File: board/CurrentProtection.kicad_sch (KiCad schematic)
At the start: 26 parts, among them Q4 IPB180N10S4-02, Q9 IPB180N10S4-02, U10 ACS72981LLRATR-100U3, U2 LM5050MK-1_NOPB, U3 LM5050MK-1_NOPB

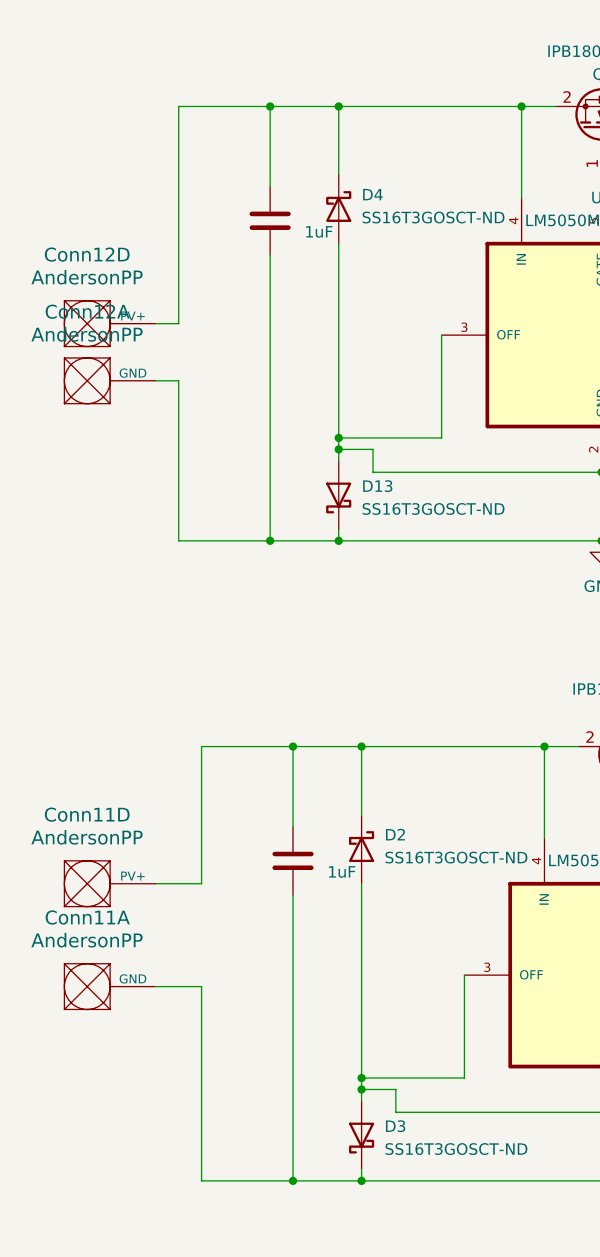
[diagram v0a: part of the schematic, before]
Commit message: new connectors
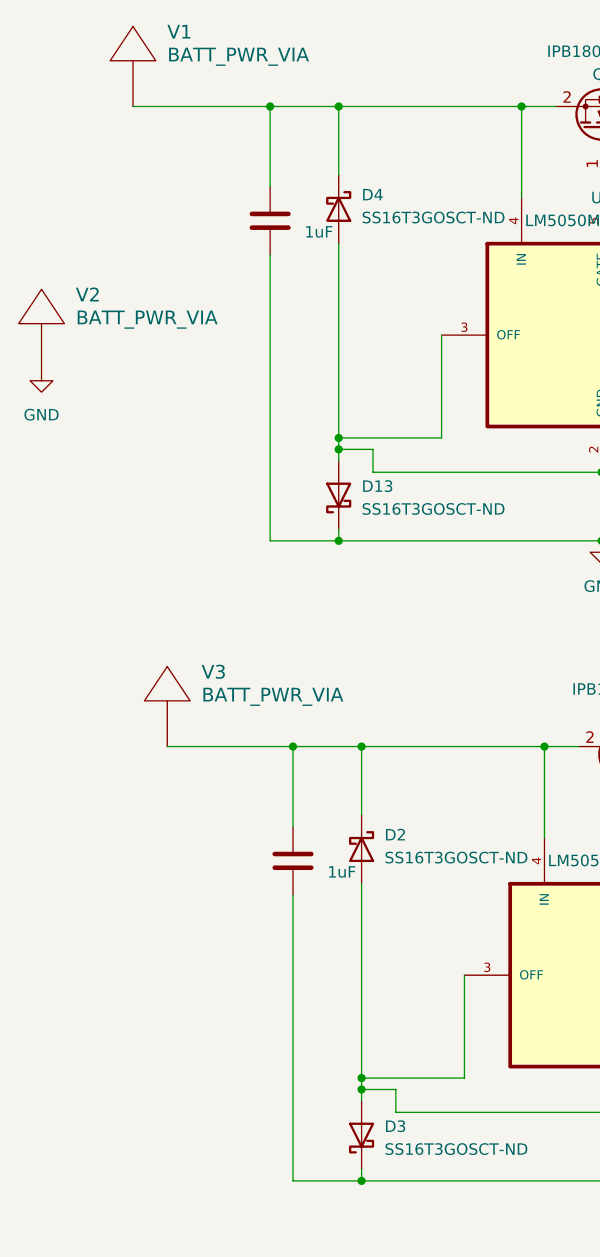
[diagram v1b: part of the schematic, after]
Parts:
- removed Conn11, Conn12: AndersonPP, MRDT_Connectors:Square_Anderson_2_H_Side_By_Side_PV, symbol MRDT_Connectors:AndersonPP
- added V1, V2, V3: BATT_PWR_VIA, MRDT_Drill_Holes:BATT_PWR_VIA, symbol MRDT_Drill_Holes:BATT_PWR_VIA
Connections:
- net GND: now also V2.1
- net at C11.1, D4.1 (K), Q4.2 (S)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: now also V1.1
- net at C5.1, D2.1 (K), Q9.2 (S)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: now also V3.1

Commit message: Deleted Capacitors
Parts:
- removed C13, C4: 22uF, Capacitor_SMD:C_0603_1608Metric_Pad1.08x0.95mm_HandSolder, symbol Device:C
- added C13, C24, C4: 1000uF, Capacitor_THT:CP_Radial_D16.0mm_P7.50mm, symbol Device:C_Polarized_US
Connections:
- net GND: now also C13.2, C24.2, C4.2
- net at D14.1 (K), D5.1 (K), Q4.4 (D)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: now also C13.1, C24.1, C4.1
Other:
- moved on the sheet: C1, C2, R1, U10

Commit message: experimented with layout
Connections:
- net Batt2: now reaches C5.1, D2.1 (K), Q9.2 (S), Q9.3 (S), Q9.5 (S), Q9.6 (S), Q9.7 (S), U3.4 (IN), V3.1
- net Batt1: now reaches C11.1, D4.1 (K), Q4.2 (S), Q4.3 (S), Q4.5 (S), Q4.6 (S), Q4.7 (S), U2.4 (IN), V1.1
- net Batt_to_CS: now reaches C13.1, C24.1, C4.1, D14.1 (K), D5.1 (K), Q4.4 (D), Q9.4 (D), R2.2, R39.2, U10.5 (IP+), U2.6 (OUT), U3.6 (OUT)
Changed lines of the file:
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@@
+		)
+	)
+	(label "Batt_to_CS"
+		(at 199.39 73.66 0)
+		(effects
+			(font
+				(size 1.27 1.27)
+			)
+			(justify left bottom)
+		)
+	)
+	(label "Batt1"
+		(at 33.02 73.66 0)
+		(effects
+			(font
+				(size 1.27 1.27)
+			)
+			(justify left bottom)
+		)
+	)
+	(label "Batt2"
+		(at 35.56 144.78 0)
+		(effects
+			(font
+				(size 1.27 1.27)
+			)
+			(justify left bottom)
 		)
 	)

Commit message: do basically everything
12 hours of our life
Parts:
- removed C10, C12: 0.1uF, Capacitor_SMD:C_0603_1608Metric_Pad1.08x0.95mm_HandSolder, symbol Device:C
- removed C11, C5: 1uF, Capacitor_SMD:C_0603_1608Metric_Pad1.08x0.95mm_HandSolder, symbol Device:C
- removed D13, D2, D3, D4: SS16T3GOSCT-ND, Diode_SMD:D_SMA, symbol Diode:SS16
- removed D14, D5: SMBJ60AFSTR-ND, Diode_SMD:D_SMB, symbol Diode:SS16
- removed Q4, Q9: IPB180N10S4-02, Package_TO_SOT_SMD:TO-263-6, symbol Transistor_FET:IPB180N10S4-02
- removed R2: R_US, Resistor_SMD:R_0603_1608Metric_Pad0.98x0.95mm_HandSolder, symbol Device:R_US
- removed R39: 100, Resistor_SMD:R_0603_1608Metric_Pad0.98x0.95mm_HandSolder, symbol Device:R_US
- removed U2, U3: LM5050MK-1_NOPB, PowerManagementBoard:SOT95P280X110-6N, symbol LM5050MK-1_NOPB:LM5050MK-1_NOPB
- removed V3: BATT_PWR_VIA, MRDT_Drill_Holes:BATT_PWR_VIA, symbol MRDT_Drill_Holes:BATT_PWR_VIA
- added TP1: TestPoint, Connector_Pin:Pin_D1.1mm_L10.2mm_W3.5mm_Flat, symbol Connector:TestPoint
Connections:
- net Batt_to_CS is gone; now on net Batt1: C13.1, C24.1, C4.1, U10.5 (IP+)
- net +24V: now also TP1.1

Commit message: 17 hours of our lives
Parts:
- D6: value GRNLED -> GRN
- TP1: footprint Connector_Pin:Pin_D1.1mm_L10.2mm_W3.5mm_Flat -> TestPoint:TestPoint_Pad_D1.0mm
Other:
- moved on the sheet: V1
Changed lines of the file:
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@@
+	)
+	(junction
+		(at 260.35 88.9)
+		(diameter 0)
+		(color 0 0 0 0)
+	)
+	(junction
+		(at 168.91 81.28)
+		(diameter 0)
+		(color 0 0 0 0)
+	)
+	(junction
+		(at 168.91 73.66)
+		(diameter 0)
+		(color 0 0 0 0)
 	)
 	(junction
@@
 	)
 	(junction
-		(at 260.35 88.9)
-		(diameter 0)
-		(color 0 0 0 0)
-	)
-	(junction
-		(at 168.91 81.28)
-		(diameter 0)
-		(color 0 0 0 0)
-	)
-	(junction
-		(at 168.91 73.66)
-		(diameter 0)
-		(color 0 0 0 0)
-	)
-	(junction
 		(at 241.3 109.22)
 		(diameter 0)
@@
 	(wire
 		(pts
+			(xy 153.67 73.66) (xy 63.5 73.66)
+		)
+		(stroke
+			(width 0)
+			(type default)
+		)
+	)
+	(wire
+		(pts
 			(xy 168.91 73.66) (xy 182.88 73.66)
 		)
@@
 		(pts
 			(xy 264.16 109.22) (xy 264.16 110.49)
-		)
-		(stroke
-			(width 0)
-			(type default)
-		)
-	)
-	(wire
-		(pts
-			(xy 26.67 73.66) (xy 153.67 73.66)
 		)
 		(stroke
@@
 	)
 	(label "Batt1"
-		(at 33.02 73.66 0)
+		(at 153.67 73.66 0)
 		(effects
 			(font
@@
 			)
 		)
-		(property "Value" "GRNLED"
+		(property "Value" "GRN"
 			(at 190.8175 137.16 0)
 			(effects
@@
 			)
 		)
-		(property "Footprint" "Connector_Pin:Pin_D1.1mm_L10.2mm_W3.5mm_Flat"
+		(property "Footprint" "TestPoint:TestPoint_Pad_D1.0mm"
 			(at 214.63 101.6 0)
 			(effects
@@
 	(symbol
 		(lib_id "MRDT_Drill_Holes:BATT_PWR_VIA")
-		(at 26.67 68.58 0)
+		(at 63.5 68.58 0)
 		(unit 1)
 		(exclude_from_sim no)
@@
 		(fields_autoplaced yes)
 		(property "Reference" "V1"
-			(at 30.48 65.4049 0)
+			(at 67.31 65.4049 0)
 			(effects
 				(font
@@
 		)
 		(property "Value" "BATT_PWR_VIA"
-			(at 30.48 67.9449 0)
+			(at 67.31 67.9449 0)
 			(effects
 				(font
@@
 		)
 		(property "Footprint" "MRDT_Drill_Holes:BATT_PWR_VIA"
-			(at 26.67 68.58 0)
+			(at 63.5 68.58 0)
 			(effects
 				(font
@@
 		)
 		(property "Datasheet" ""
-			(at 26.67 68.58 0)
+			(at 63.5 68.58 0)
 			(effects
 				(font
@@
 		)
 		(property "Description" ""
-			(at 26.67 68.58 0)
-			(effects
-				(font
+			(at 63.5 68.58 0)
+			(effects
+				(font

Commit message: 18 Hours and counting...
-Moved LEDs,
-Added innocent kitties
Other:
- moved on the sheet: V1
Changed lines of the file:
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@@
 	(wire
 		(pts
-			(xy 153.67 73.66) (xy 63.5 73.66)
+			(xy 153.67 73.66) (xy 140.97 73.66)
 		)
 		(stroke
@@
 	(symbol
 		(lib_id "MRDT_Drill_Holes:BATT_PWR_VIA")
-		(at 63.5 68.58 0)
+		(at 140.97 68.58 0)
 		(unit 1)
 		(exclude_from_sim no)
@@
 		(fields_autoplaced yes)
 		(property "Reference" "V1"
-			(at 67.31 65.4049 0)
+			(at 144.78 65.4049 0)
 			(effects
 				(font
@@
 		)
 		(property "Value" "BATT_PWR_VIA"
-			(at 67.31 67.9449 0)
+			(at 144.78 67.9449 0)
 			(effects
 				(font
@@
 		)
 		(property "Footprint" "MRDT_Drill_Holes:BATT_PWR_VIA"
-			(at 63.5 68.58 0)
+			(at 140.97 68.58 0)
 			(effects
 				(font
@@
 		)
 		(property "Datasheet" ""
-			(at 63.5 68.58 0)
+			(at 140.97 68.58 0)
 			(effects
 				(font
@@
 		)
 		(property "Description" ""
-			(at 63.5 68.58 0)
-			(effects
-				(font
+			(at 140.97 68.58 0)
+			(effects
+				(font

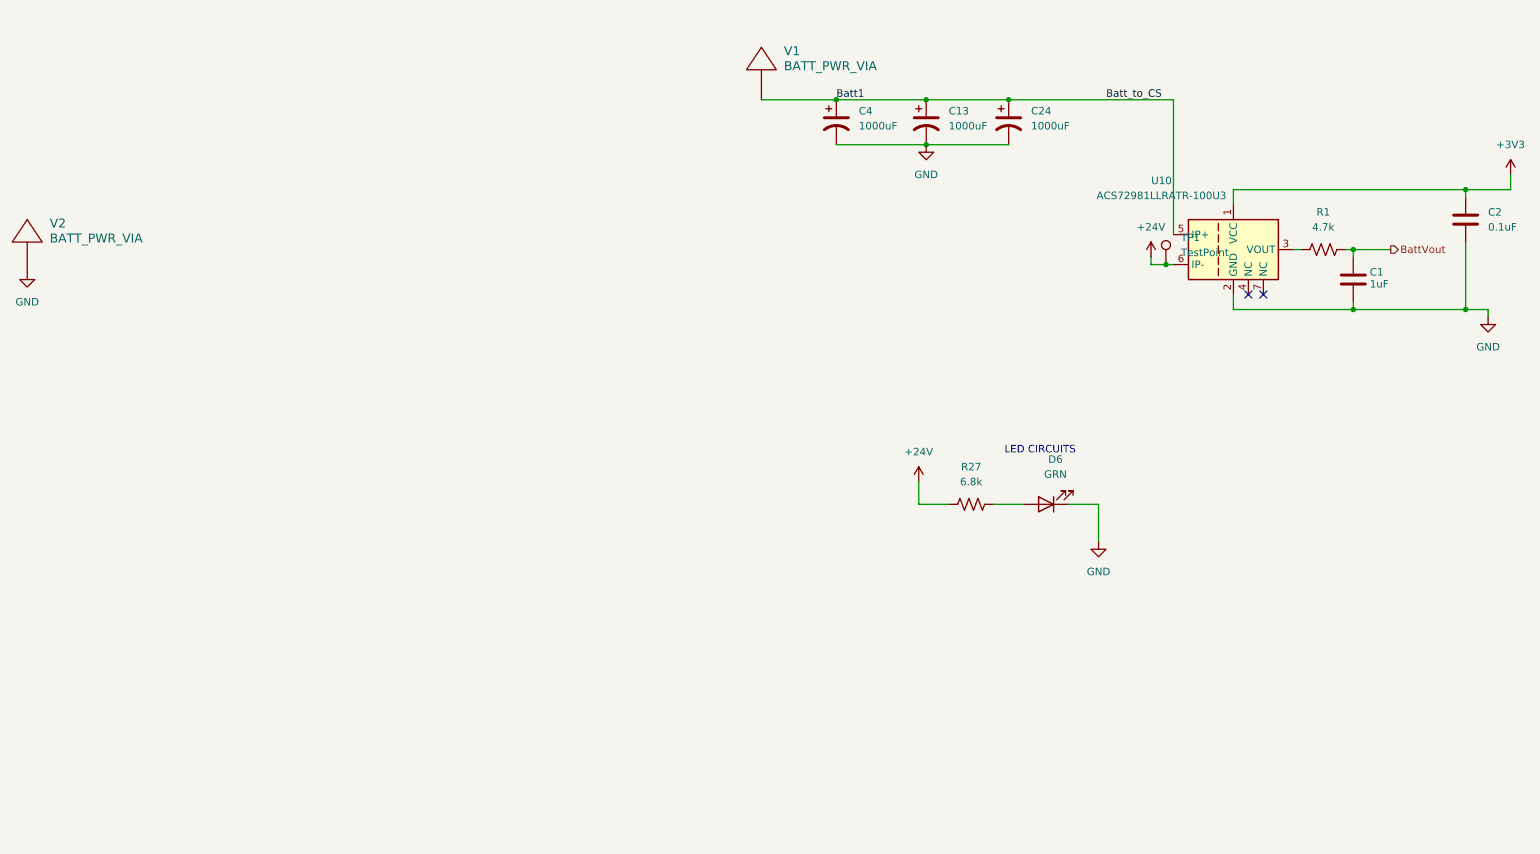
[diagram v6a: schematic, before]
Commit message: Center schematics and layout for prettiness
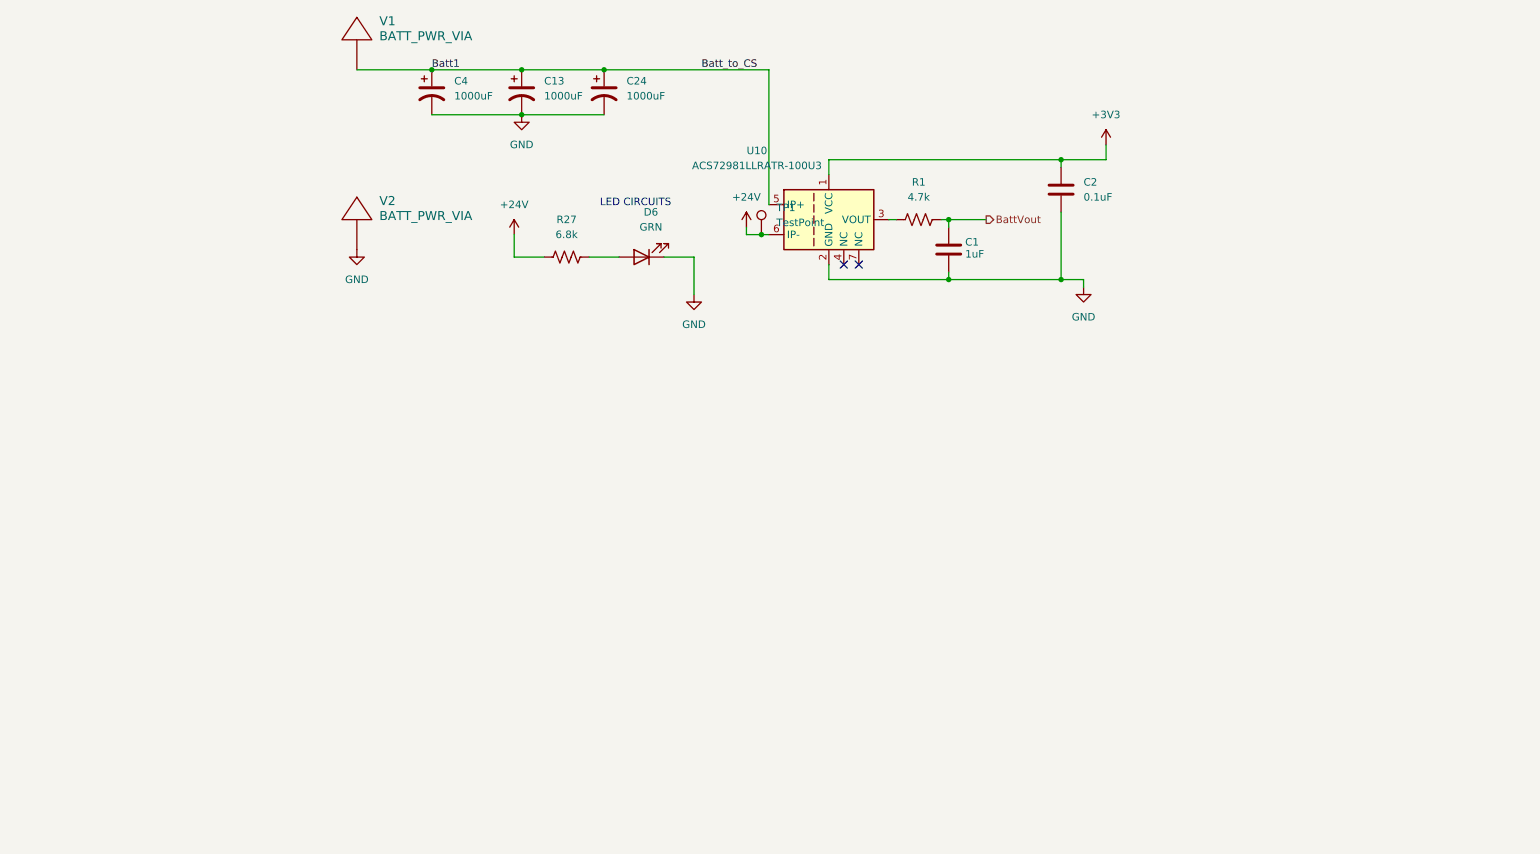
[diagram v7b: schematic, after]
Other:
- moved on the sheet: C1, C13, C2, C24, C4, D6, R1, R27, TP1, U10, V1, V2

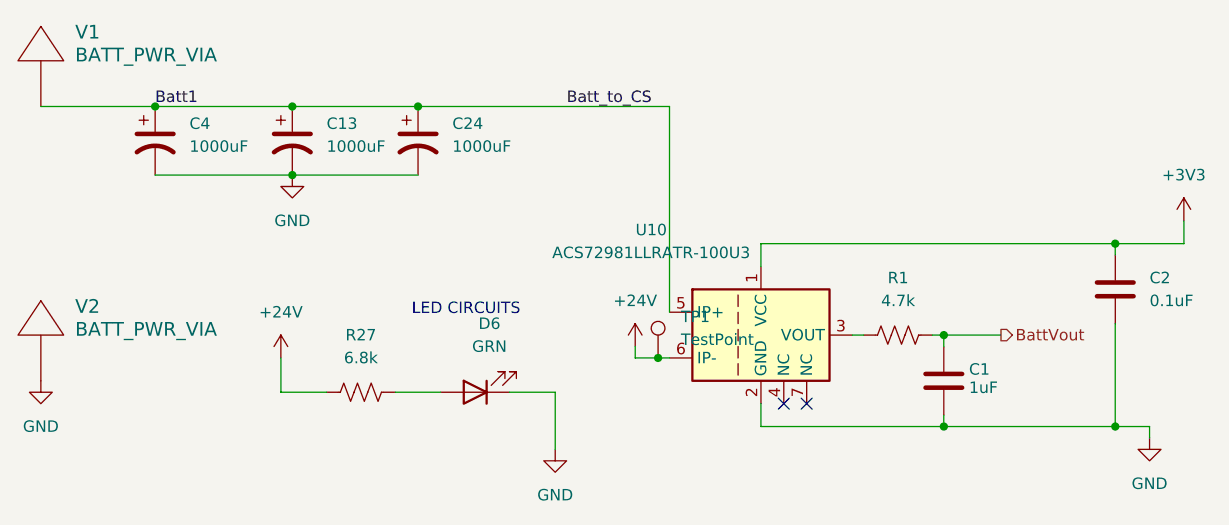
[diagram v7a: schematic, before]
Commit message: add label for battery sensing molex connector
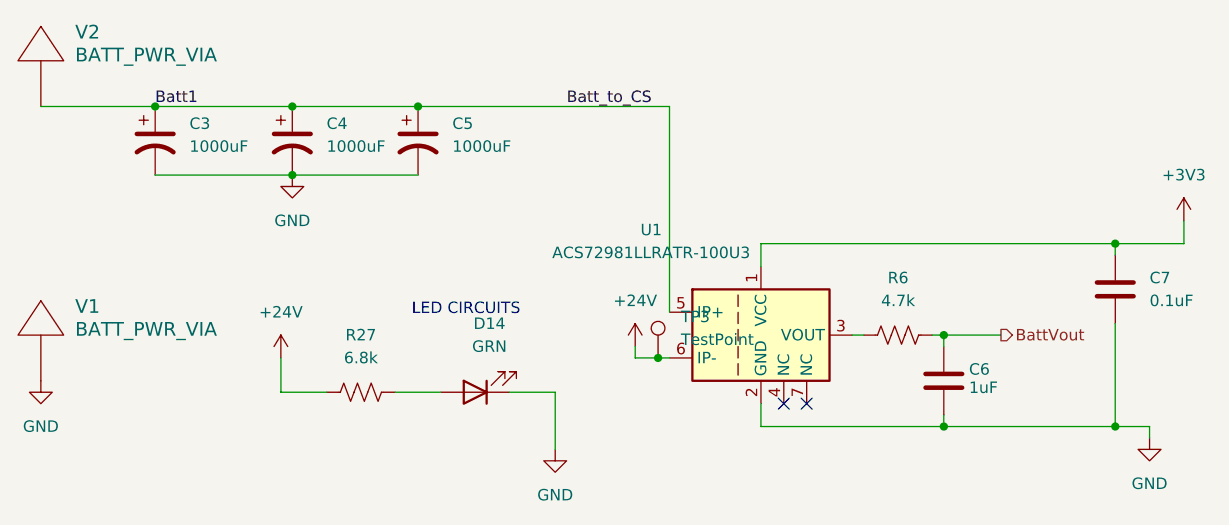
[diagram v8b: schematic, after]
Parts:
- renumbered C4 to C3, C13 to C4, C24 to C5, C1 to C6, C2 to C7, D6 to D14, R1 to R6, TP1 to TP3, U10 to U1, V2 to V1, V1 to V2
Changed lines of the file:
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@@
 		(dnp no)
 		(fields_autoplaced yes)
-		(property "Reference" "C2"
+		(property "Reference" "C7"
 			(at 195.58 87.6299 0)
 			(effects
@@
 			(project ""
 				(path "/7eaa639d-7062-45e7-be05-1c2855431307/fa17e088-8bc3-4875-b327-c5ed0adaa270"
-					(reference "C2")
+					(reference "C7")
 					(unit 1)
 				)
@@
 		(dnp no)
 		(fields_autoplaced yes)
-		(property "Reference" "C24"
+		(property "Reference" "C5"
 			(at 118.11 70.4849 0)
 			(effects
@@
 			(project "PowerManagementBoard"
 				(path "/7eaa639d-7062-45e7-be05-1c2855431307/fa17e088-8bc3-4875-b327-c5ed0adaa270"
-					(reference "C24")
+					(reference "C5")
 					(unit 1)
 				)
@@
 		(dnp no)
 		(fields_autoplaced yes)
-		(property "Reference" "D6"
+		(property "Reference" "D14"
 			(at 122.2375 92.71 0)
 			(effects
@@
 			(project "PowerManagementBoard"
 				(path "/7eaa639d-7062-45e7-be05-1c2855431307/fa17e088-8bc3-4875-b327-c5ed0adaa270"
-					(reference "D6")
+					(reference "D14")
 					(unit 1)
 				)
@@
 		(dnp no)
 		(fields_autoplaced yes)
-		(property "Reference" "TP1"
+		(property "Reference" "TP3"
 			(at 143.51 91.9479 0)
 			(effects
@@
 			(project ""
 				(path "/7eaa639d-7062-45e7-be05-1c2855431307/fa17e088-8bc3-4875-b327-c5ed0adaa270"
-					(reference "TP1")
+					(reference "TP3")
 					(unit 1)
 				)
@@
 		(on_board yes)
 		(dnp no)
-		(property "Reference" "C1"
+		(property "Reference" "C6"
 			(at 175.514 97.79 0)
 			(effects
@@
 			(project ""
 				(path "/7eaa639d-7062-45e7-be05-1c2855431307/fa17e088-8bc3-4875-b327-c5ed0adaa270"
-					(reference "C1")
+					(reference "C6")
 					(unit 1)
 				)
@@
 		(dnp no)
 		(fields_autoplaced yes)
-		(property "Reference" "C4"
+		(property "Reference" "C3"
 			(at 88.9 70.4849 0)
 			(effects
@@
 			(project ""
 				(path "/7eaa639d-7062-45e7-be05-1c2855431307/fa17e088-8bc3-4875-b327-c5ed0adaa270"
-					(reference "C4")
+					(reference "C3")
 					(unit 1)
 				)
@@
 		(dnp no)
 		(fields_autoplaced yes)
-		(property "Reference" "V2"
+		(property "Reference" "V1"
 			(at 76.2 90.8049 0)
 			(effects
@@
 			(project "PowerManagementBoard"
 				(path "/7eaa639d-7062-45e7-be05-1c2855431307/fa17e088-8bc3-4875-b327-c5ed0adaa270"
-					(reference "V2")
+					(reference "V1")
 					(unit 1)
 				)
@@
 		(dnp no)
 		(fields_autoplaced yes)
-		(property "Reference" "C13"
+		(property "Reference" "C4"
 			(at 104.14 70.4849 0)
 			(effects
@@
 			(project "PowerManagementBoard"
 				(path "/7eaa639d-7062-45e7-be05-1c2855431307/fa17e088-8bc3-4875-b327-c5ed0adaa270"
-					(reference "C13")
+					(reference "C4")
 					(unit 1)
 				)
@@
 		(dnp no)
 		(fields_autoplaced yes)
-		(property "Reference" "R1"
+		(property "Reference" "R6"
 			(at 167.64 87.63 90)
 			(effects
@@
 			(project ""
 				(path "/7eaa639d-7062-45e7-be05-1c2855431307/fa17e088-8bc3-4875-b327-c5ed0adaa270"
-					(reference "R1")
+					(reference "R6")
 					(unit 1)
 				)
@@
 		(on_board yes)
 		(dnp no)
-		(property "Reference" "U10"
+		(property "Reference" "U1"
 			(at 140.208 82.296 0)
 			(effects
@@
 			(project ""
 				(path "/7eaa639d-7062-45e7-be05-1c2855431307/fa17e088-8bc3-4875-b327-c5ed0adaa270"
-					(reference "U10")
+					(reference "U1")
 					(unit 1)
 				)
@@
 		(dnp no)
 		(fields_autoplaced yes)
-		(property "Reference" "V1"
+		(property "Reference" "V2"
 			(at 76.2 60.3249 0)
 			(effects
@@
 			(project ""
 				(path "/7eaa639d-7062-45e7-be05-1c2855431307/fa17e088-8bc3-4875-b327-c5ed0adaa270"
-					(reference "V1")
-					(unit 1)
-				)
+					(reference "V2")
+					(unit 1)
+				)
